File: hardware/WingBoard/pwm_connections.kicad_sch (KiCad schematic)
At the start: 32 parts, among them J401 PWM_IN1, J402 PWM_IN2, J403 PWM_IN3, J404 PWM_IN4, J405 PWM_IN5, J406 PWM_IN6, J407 PWM_OUT1, J408 PWM_OUT2, J409 PWM_OUT3, J410 PWM_OUT4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

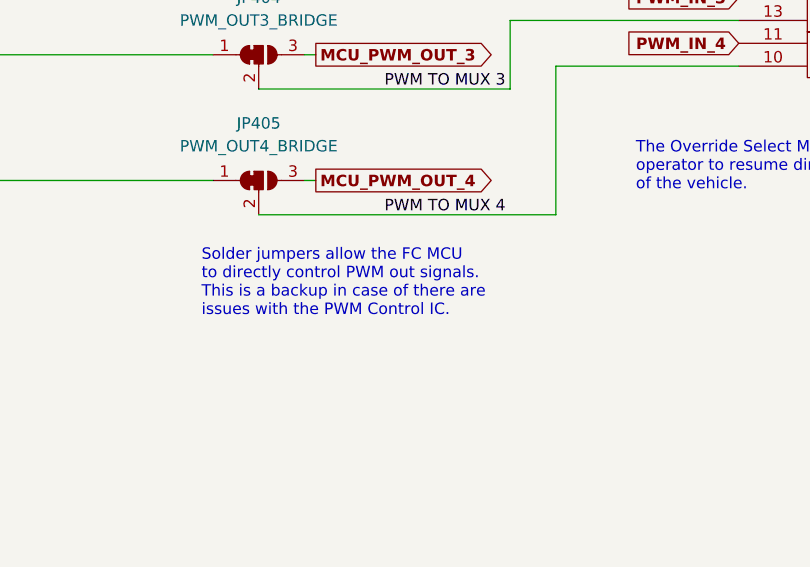
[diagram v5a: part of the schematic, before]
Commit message: Final wingboard v0.1 hardware design.
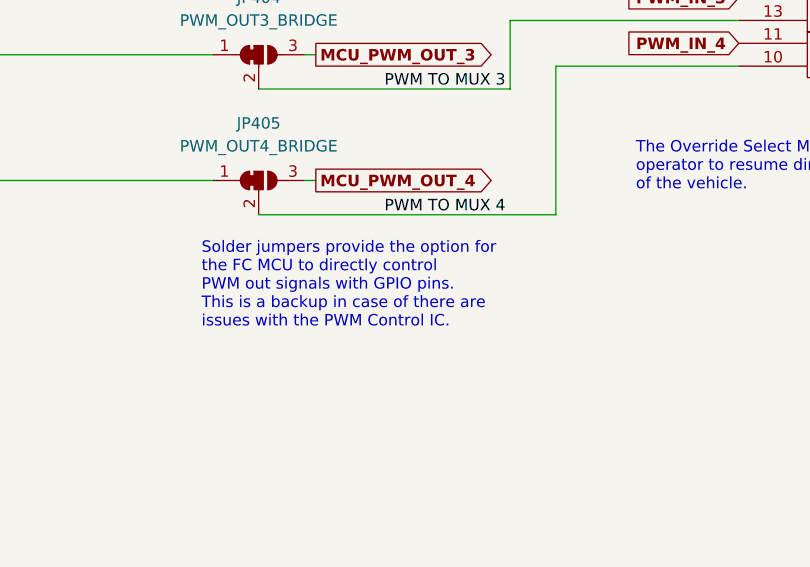
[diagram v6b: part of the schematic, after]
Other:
- note added: "Solder jumpers provide the option for the FC MCU to directly control PWM out signals with GPIO pins. This is a backup in case of there are issues with the PWM Control IC."
- note removed: "Solder jumpers allow the FC MCU to directly control PWM out signals. This is a backup in case of there are issues with the PWM Control IC."
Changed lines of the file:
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@@
     (effects (font (size 2 2) bold) (justify left bottom))
   )
-  (text "Solder jumpers allow the FC MCU\nto directly control PWM out signals.\nThis is a backup in case of there are \nissues with the PWM Control IC."
-    (at 158.75 109.22 0)
+  (text "Solder jumpers provide the option for\nthe FC MCU to directly control \nPWM out signals with GPIO pins.\nThis is a backup in case of there are \nissues with the PWM Control IC."
+    (at 158.75 110.49 0)
     (effects (font (size 1.27 1.27)) (justify left bottom))
   )
